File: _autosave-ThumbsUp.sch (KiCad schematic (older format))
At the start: 152 parts, among them IC1 RP2040, IC2 W25Q128JVSIM, IC3 RP2040, IC4 W25Q128JVSIM, J1 Conn_01x04_Male, J10 Raiser_Male, J11 Raiser_Female, J12 Raiser_Male, J13 Raiser_Female, J14 Raiser_Male, J15 Raiser_Female, J16 Raiser_Male, J17 Raiser_Female, J18 Raiser_Male, J19 Raiser_Female, J2 Conn_01x04_Male, J20 Conn_01x04_Female, J21 Conn_01x04_Female, J22 Conn_01x04_Female, J23 Conn_01x04_Female, J24 Conn_01x04_Male, J25 Conn_01x04_Male, J26 Conn_01x04_Male, J27 Conn_01x04_Male, J28 Conn_01x04_Female, J29 Conn_01x04_Female, J3 Conn_01x04_Female, J30 Conn_01x04_Female, J31 Conn_01x04_Female, J32 USB_C_Receptacle_USB2.0, J33 Raiser_Male, J34 Raiser_Female, J35 Raiser_Male, J36 STX-3501-3N, J37 USB_C_Receptacle_USB2.0, J38 Raiser_Female, J39 Raiser_Male, J4 Conn_01x04_Male, J40 Raiser_Female, J41 Raiser_Male, J42 Raiser_Female, J43 Raiser_Male, J44 Raiser_Female, J45 Raiser_Male, J46 STX-3501-3N, J5 Conn_01x04_Female, J6 Conn_01x04_Male, J7 Conn_01x04_Male, J8 Conn_01x04_Male, J9 Raiser_Female, U1 NCP1117-3.3_SOT223, U2 NCP1117-3.3_SOT223, Y1 ABLS-12.000MHZ-B4-T, Y2 ABLS-12.000MHZ-B4-T

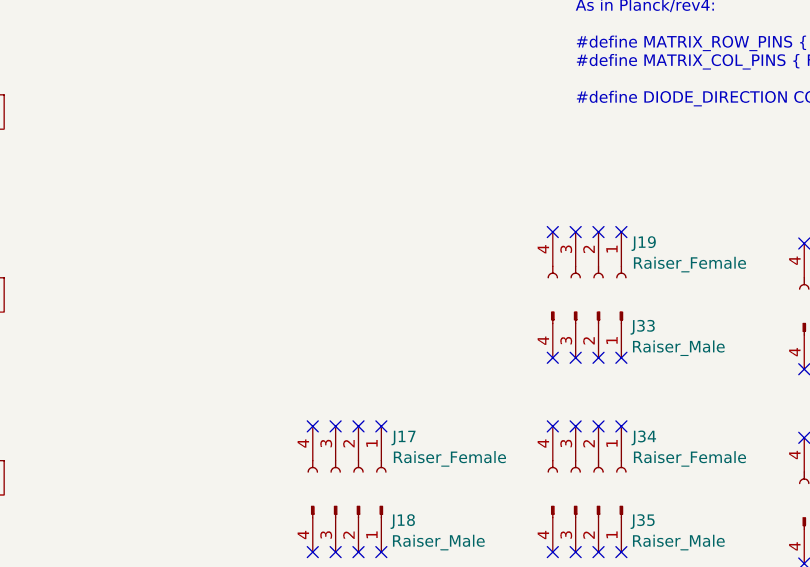
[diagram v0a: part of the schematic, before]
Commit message: Rearranged the header pins to match the actual positions.
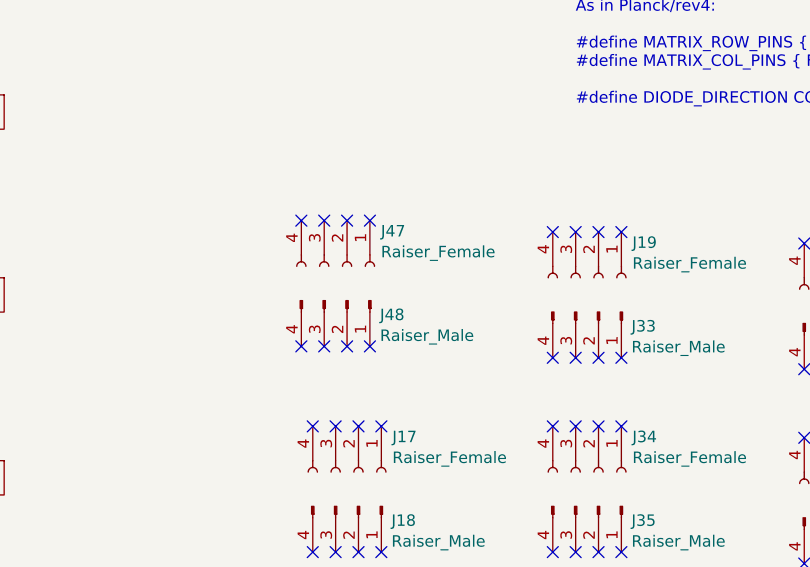
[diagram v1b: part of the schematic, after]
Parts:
- added J47: Raiser_Female, Connector_PinSocket_2.54mm:PinSocket_1x04_P2.54mm_Vertical, symbol Connector:Conn_01x04_Female
- added J48: Raiser_Male, Connector_PinHeader_2.54mm:PinHeader_1x04_P2.54mm_Vertical, symbol Connector:Conn_01x04_Male
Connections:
- no-connect marks 108 -> 116
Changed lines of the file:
@@
 	4250 8100 4550 8100
 $Comp
-L power:GND #PWR?
+L power:GND #PWR0149
 U 1 1 641658E3
 P 4850 8100
-F 0 "#PWR?" H 4850 7850 50  0001 C CNN
+F 0 "#PWR0149" H 4850 7850 50  0001 C CNN
 F 1 "GND" H 4855 7927 50  0000 C CNN
 F 2 "" H 4850 8100 50  0001 C CNN
@@
 	4650 8100 4850 8100
 $Comp
-L power:+3.3V #PWR?
+L power:+3.3V #PWR0150
 U 1 1 641956AA
 P 4850 8900
-F 0 "#PWR?" H 4850 8750 50  0001 C CNN
+F 0 "#PWR0150" H 4850 8750 50  0001 C CNN
 F 1 "+3.3V" H 4865 9073 50  0000 C CNN
 F 2 "" H 4850 8900 50  0001 C CNN
@@
 	14550 8050 15000 8050
 $Comp
-L power:+3.3V #PWR?
+L power:+3.3V #PWR0151
 U 1 1 64225663
 P 15350 8850
-F 0 "#PWR?" H 15350 8700 50  0001 C CNN
+F 0 "#PWR0151" H 15350 8700 50  0001 C CNN
 F 1 "+3.3V" H 15365 9023 50  0000 C CNN
 F 2 "" H 15350 8850 50  0001 C CNN
@@
 $EndComp
 $Comp
-L power:GND #PWR?
+L power:GND #PWR0152
 U 1 1 64226D4D
 P 15350 8050
-F 0 "#PWR?" H 15350 7800 50  0001 C CNN
+F 0 "#PWR0152" H 15350 7800 50  0001 C CNN
 F 1 "GND" H 15355 7877 50  0000 C CNN
 F 2 "" H 15350 8050 50  0001 C CNN
@@
 Text GLabel 15350 8850 2    50   Input ~ 0
 R-RING1
+$Comp
+L Connector:Conn_01x04_Female J47
+U 1 1 63AC0C46
+P 18150 12650
+F 0 "J47" V 17996 12798 50  0000 L CNN
+F 1 "Raiser_Female" V 18087 12798 50  0000 L CNN
+F 2 "Connector_PinSocket_2.54mm:PinSocket_1x04_P2.54mm_Vertical" H 18150 12650 50  0001 C CNN
+F 3 "~" H 18150 12650 50  0001 C CNN
+	1    18150 12650
+	0    1    1    0
+$EndComp
+$Comp
+L Connector:Conn_01x04_Male J48
+U 1 1 63AC0C4C
+P 18150 12800
+F 0 "J48" V 18212 12944 50  0000 L CNN
+F 1 "Raiser_Male" V 18303 12944 50  0000 L CNN
+F 2 "Connector_PinHeader_2.54mm:PinHeader_1x04_P2.54mm_Vertical" H 18150 12800 50  0001 C CNN
+F 3 "~" H 18150 12800 50  0001 C CNN
+	1    18150 12800
+	0    1    1    0
+$EndComp
+NoConn ~ 17950 12450
+NoConn ~ 18050 12450
+NoConn ~ 18150 12450
+NoConn ~ 18250 12450
+NoConn ~ 17950 13000
+NoConn ~ 18050 13000
+NoConn ~ 18150 13000
+NoConn ~ 18250 13000
 $EndSCHEMATC
